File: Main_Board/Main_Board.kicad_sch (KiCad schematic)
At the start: 0 parts

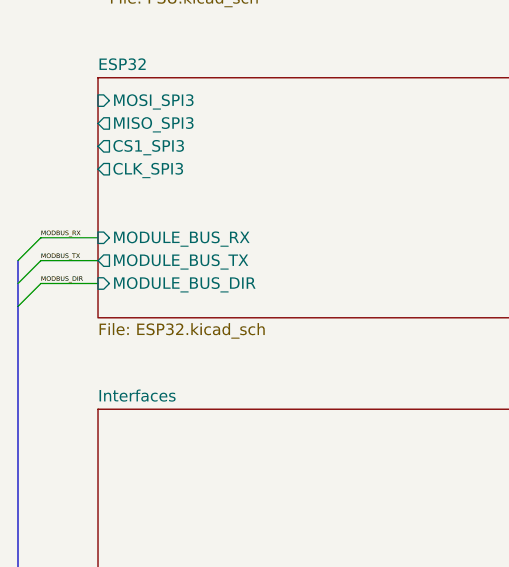
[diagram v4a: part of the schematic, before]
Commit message: add external obrds interfaces
Todo pyro chanells
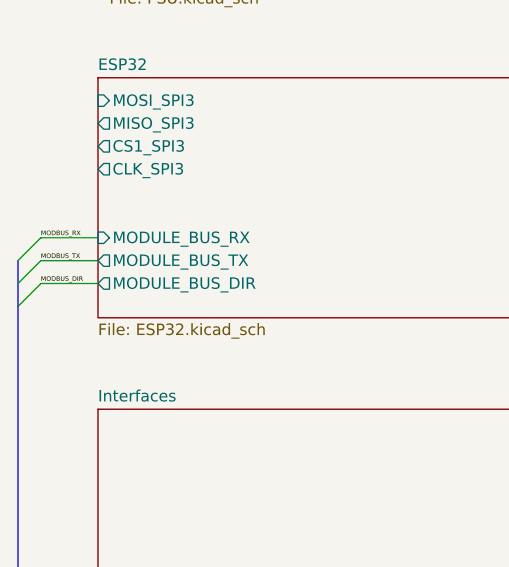
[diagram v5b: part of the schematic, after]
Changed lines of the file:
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@@
 			)
 		)
-		(pin "MODULE_BUS_DIR" input
+		(pin "MODULE_BUS_DIR" output
 			(at 189.23 96.52 180)
 			(effects
